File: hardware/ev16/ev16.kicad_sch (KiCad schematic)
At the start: 165 parts, among them CN1 Conn_05x02_Female, CN2 PJ-242, J1 USB_C_Receptacle, J10 Conn_01x03_Pin, J11 Conn_02x05_Counter_Clockwise, J2 Conn_01x02_Socket, J3 AudioJack4, J4 Conn_02x03_Odd_Even, J5 Conn_02x03_Odd_Even, J6 Conn_02x05_Counter_Clockwise, J7 Conn_02x05_Counter_Clockwise, J8 Conn_02x05_Counter_Clockwise, J9 Conn_02x05_Counter_Clockwise, Q1 2N7002, Q2 2N7002, SW1 SW_SPDT, SW2 SW_Push, SW3 SW_Push, SW4 SW_Push, SW5 SW_Push, SW6 SW_Push, SW7 SW_Push, U1 BQ21040DBV, U10 STM32F405RGTx, U2 USBLC6-2P6, U3 STM32F072CBTx, U4 CH340C, U5 TPS63060, U6 WM8960CGEFL/RV, U7 ESP32-S3-WROOM-1, U8 M24C02-RMN6TP, Y1 Crystal_GND24

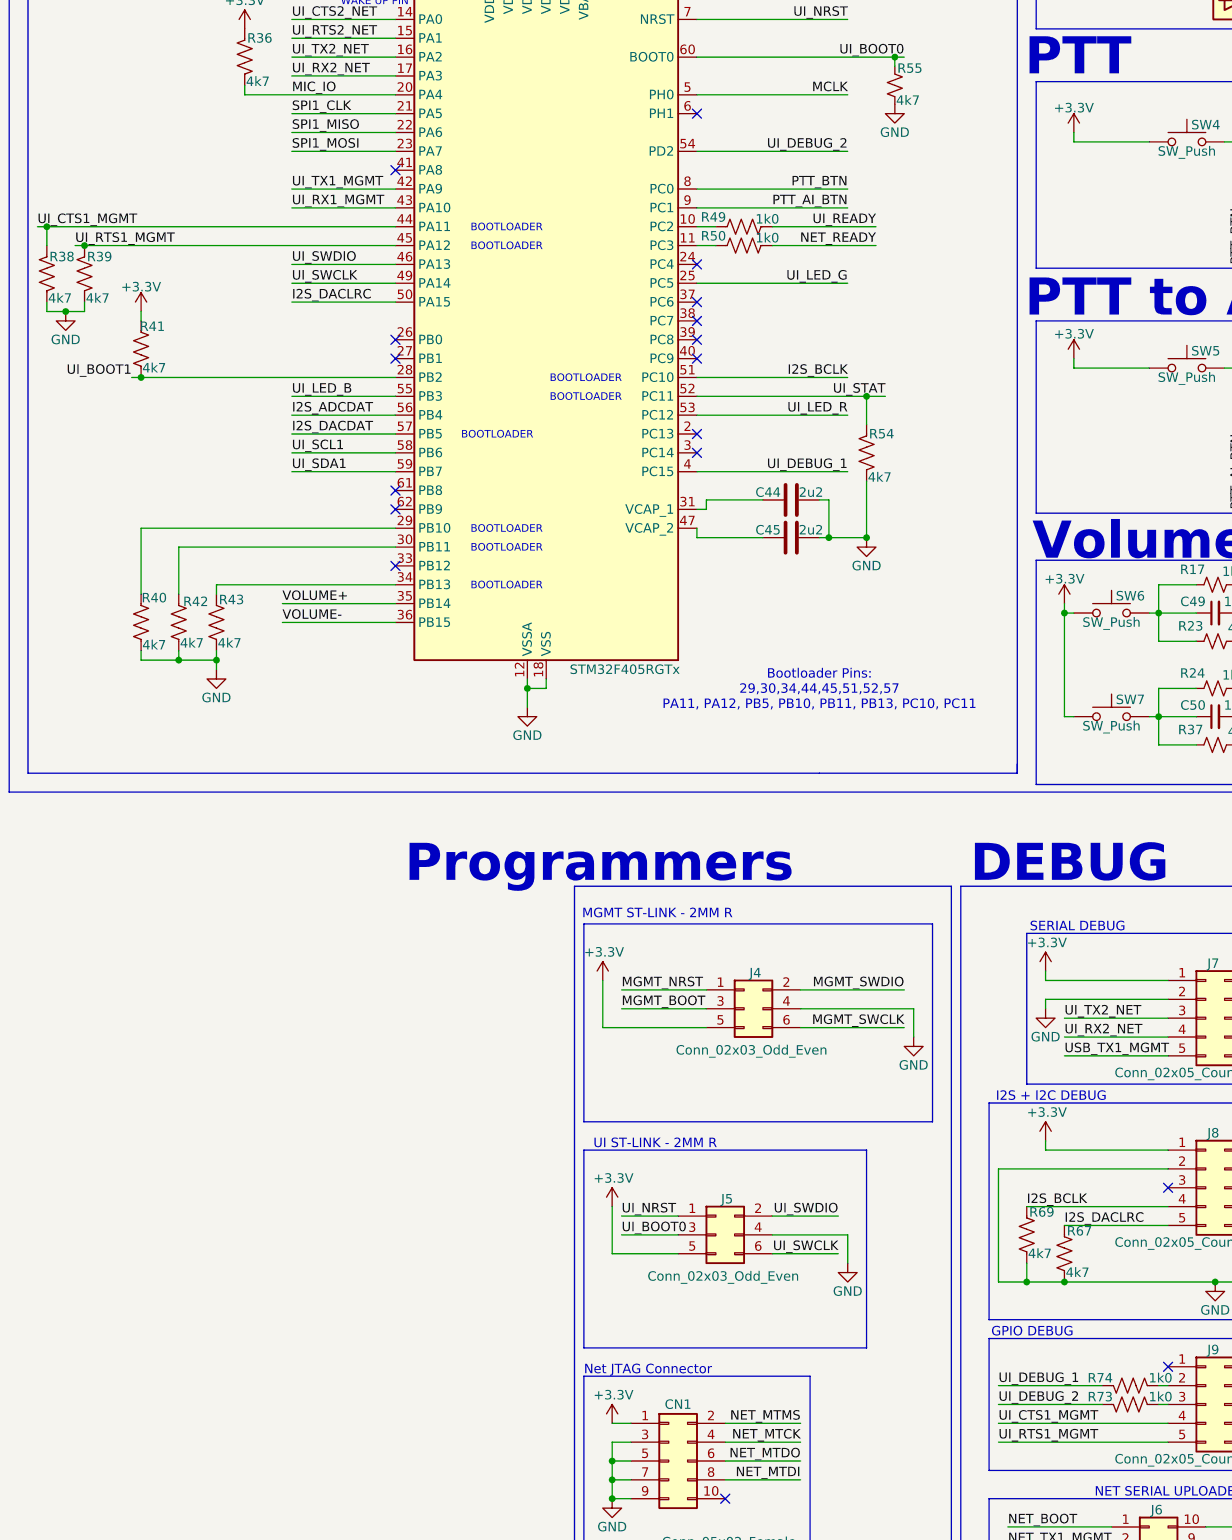
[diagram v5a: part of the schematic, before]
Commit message: stitched ground planes with vias, changed pins for volume up and down
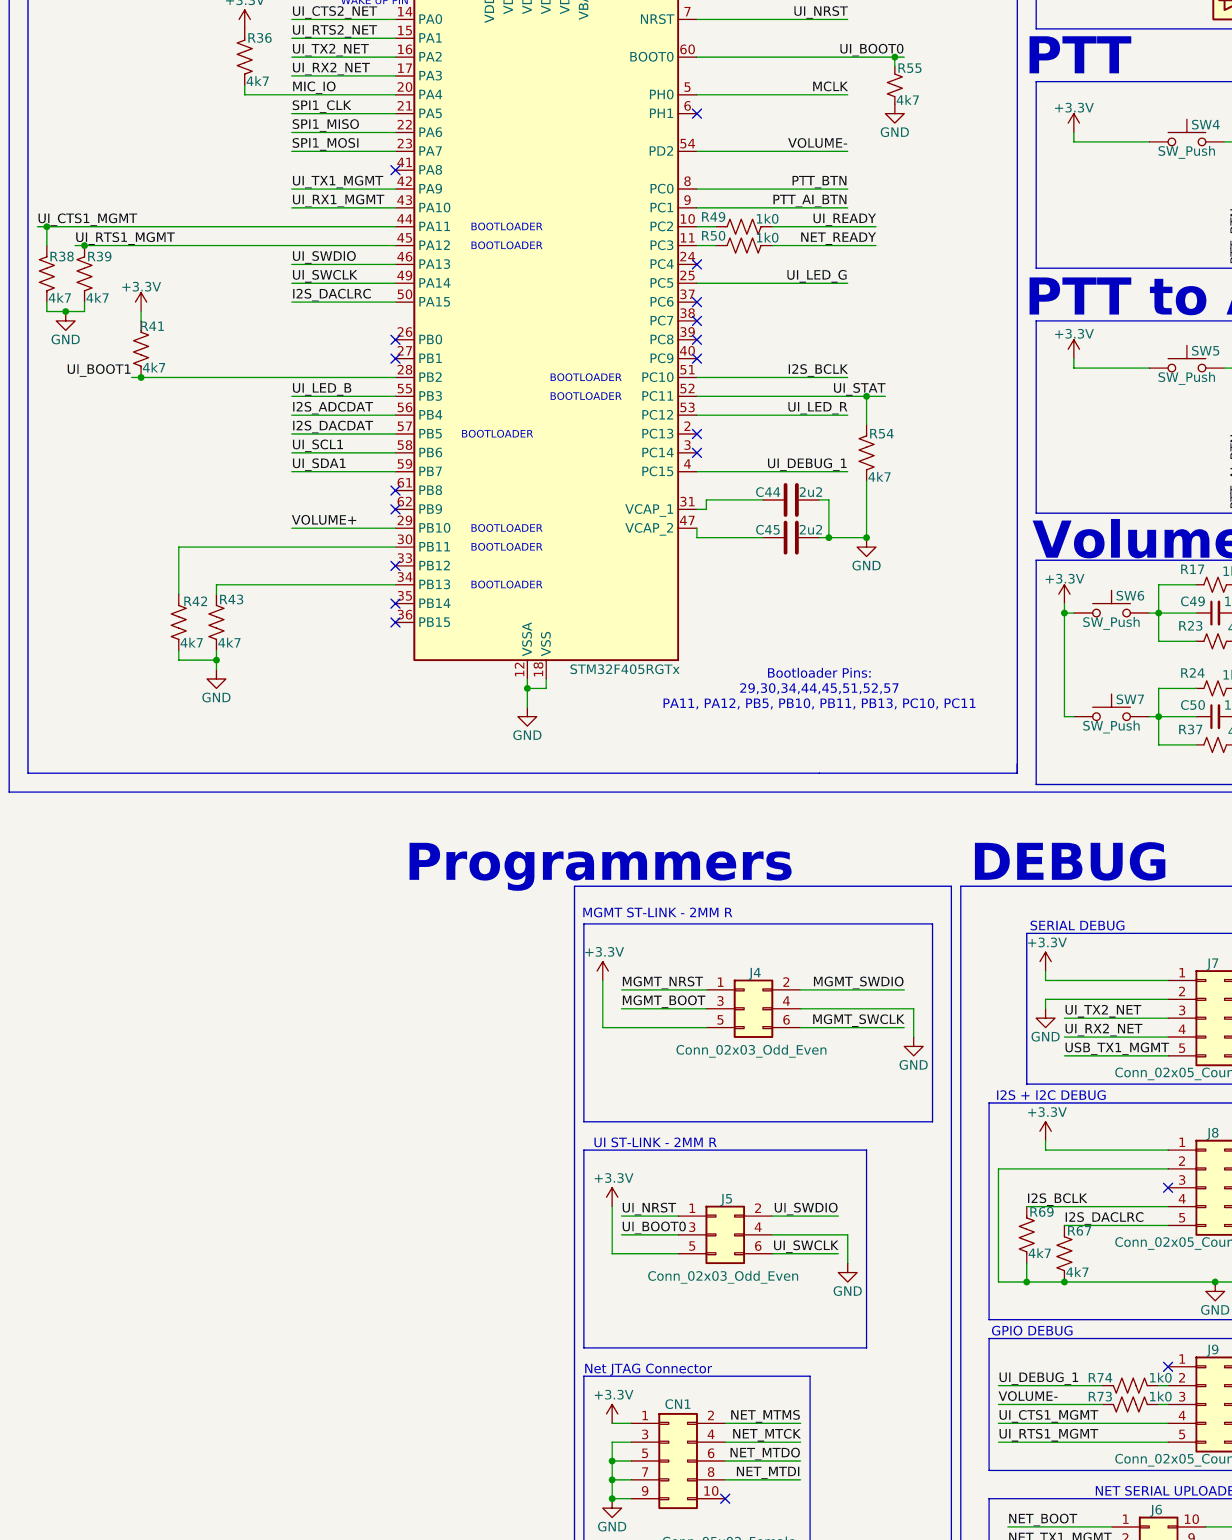
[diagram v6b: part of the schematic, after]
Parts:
- removed R40: 4k7, Resistor_SMD:R_0402_1005Metric, symbol Device:R_US
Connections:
- net UI_DEBUG_2 is gone; now on net VOLUME-: R73.2, U10.54 (PD2)
- net VOLUME+: now also U10.29 (PB10); no longer U10.35 (PB14)
- net VOLUME-: no longer U10.36 (PB15)
- no-connect marks 51 -> 53
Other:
- title: EV16 FINN BERG & BRETT REGNIER -> EV16MK1 FINN BERG & BRETT REGNIER
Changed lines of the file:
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@@
 	(paper "A2")
 	(title_block
-		(title "EV16 FINN BERG & BRETT REGNIER")
+		(title "EV16MK1 FINN BERG & BRETT REGNIER")
 		(date "2025-11-26")
-		(rev "EV16")
+		(rev "EV16MK1")
 		(company "CISCO SYSTEMS INC")
 	)
@@
 	)
 	(junction
-		(at 401.32 149.86)
-		(diameter 0)
-		(color 0 0 0 0)
-	)
-	(junction
 		(at 57.15 234.95)
 		(diameter 0)
@@
 	)
 	(no_connect
+		(at 430.53 144.78)
+	)
+	(no_connect
 		(at 57.15 247.65)
 	)
@@
 	)
 	(no_connect
+		(at 430.53 142.24)
+	)
+	(no_connect
 		(at 430.53 83.82)
 	)
@@
 	(wire
 		(pts
-			(xy 396.24 148.59) (xy 396.24 149.86)
-		)
-		(stroke
-			(width 0)
-			(type default)
-		)
-	)
-	(wire
-		(pts
 			(xy 149.86 210.82) (xy 157.48 210.82)
 		)
@@
 		)
 	)
-	(wire
-		(pts
-			(xy 396.24 132.08) (xy 430.53 132.08)
-		)
-		(stroke
-			(width 0)
-			(type default)
-		)
-	)
 	(polyline
 		(pts
@@
 	(wire
 		(pts
-			(xy 415.29 144.78) (xy 430.53 144.78)
-		)
-		(stroke
-			(width 0)
-			(type default)
-		)
-	)
-	(wire
-		(pts
 			(xy 214.63 219.71) (xy 228.6 219.71)
 		)
@@
 	(wire
 		(pts
-			(xy 415.29 142.24) (xy 430.53 142.24)
-		)
-		(stroke
-			(width 0)
-			(type default)
-		)
-	)
-	(wire
-		(pts
 			(xy 57.15 217.17) (xy 57.15 219.71)
 		)
@@
 	(wire
 		(pts
-			(xy 396.24 140.97) (xy 396.24 132.08)
-		)
-		(stroke
-			(width 0)
-			(type default)
-		)
-	)
-	(wire
-		(pts
 			(xy 287.02 200.66) (xy 292.1 200.66)
 		)
@@
 	(wire
 		(pts
-			(xy 396.24 149.86) (xy 401.32 149.86)
-		)
-		(stroke
-			(width 0)
-			(type default)
-		)
-	)
-	(wire
-		(pts
 			(xy 553.72 110.49) (xy 544.83 110.49)
 		)
@@
 	(wire
 		(pts
+			(xy 416.56 132.08) (xy 430.53 132.08)
+		)
+		(stroke
+			(width 0)
+			(type default)
+		)
+	)
+	(wire
+		(pts
 			(xy 147.32 140.97) (xy 147.32 143.51)
 		)
@@
 		)
 	)
-	(label "UI_DEBUG_2"
-		(at 511.81 250.19 0)
-		(effects
-			(font
-				(size 1.27 1.27)
-			)
-			(justify left bottom)
-		)
-	)
 	(label "LEDA_R"
 		(at 170.18 69.85 180)
@@
 		)
 	)
-	(label "VOLUME+"
-		(at 415.29 142.24 0)
-		(effects
-			(font
-				(size 1.27 1.27)
-			)
-			(justify left bottom)
-		)
-	)
 	(label "UI_SWDIO"
 		(at 490.22 224.79 180)
@@
 		)
 	)
-	(label "VOLUME-"
-		(at 415.29 144.78 0)
+	(label "BATTERY_MON"
+		(at 49.53 111.76 0)
 		(effects
 			(font
@@
 		)
 	)
-	(label "BATTERY_MON"
-		(at 49.53 111.76 0)
+	(label "UI_BOOT0"
+		(at 461.01 227.33 0)
 		(effects
 			(font
@@
 		)
 	)
-	(label "UI_BOOT0"
-		(at 461.01 227.33 0)
+	(label "VOLUME-"
+		(at 491.49 81.28 180)
 		(effects
 			(font
 				(size 1.27 1.27)
 			)
-			(justify left bottom)
+			(justify right bottom)
 		)
 	)
@@
 		)
 	)
+	(label "VOLUME+"
+		(at 416.56 132.08 0)
+		(effects
+			(font
+				(size 1.27 1.27)
+			)
+			(justify left bottom)
+		)
+	)
 	(label "NET_DEBUG_1"
 		(at 232.41 101.6 0)
@@
 		)
 	)
+	(label "VOLUME-"
+		(at 511.81 250.19 0)
+		(effects
+			(font
+				(size 1.27 1.27)
+			)
+			(justify left bottom)
+		)
+	)
 	(label "MIC_P"
 		(at 283.21 223.52 0)
@@
 		)
 	)
-	(label "UI_DEBUG_2"
-		(at 491.49 81.28 180)
-		(effects
-			(font
-				(size 1.27 1.27)
-			)
-			(justify right bottom)
-		)
-	)
 	(label "LEDA_R"
 		(at 116.84 93.98 180)
@@
 					(unit 1)
 				)
-			)
-		)
-	)
-	(symbol
-		(lib_id "Device:R_US")
-		(at 396.24 144.78 180)
-		(unit 1)
-		(exclude_from_sim no)
-		(in_bom yes)
-		(on_board yes)
-		(dnp no)
-		(property "Reference" "R40"
-			(at 398.018 141.478 0)
-			(effects
-				(font
-					(size 1.27 1.27)
-				)
-			)
-		)
-		(property "Value" "4k7"
-			(at 398.018 147.828 0)
-			(effects
-				(font
-					(size 1.27 1.27)
-				)
-			)
-		)
-		(property "Footprint" "Resistor_SMD:R_0402_1005Metric"
-			(at 398.018 144.78 90)
-			(effects
-				(font
-					(size 1.27 1.27)
-				)
-				(hide yes)
-			)
-		)
-		(property "Datasheet" "~"
-			(at 396.24 144.78 0)
-			(effects
-				(font
-					(size 1.27 1.27)
-				)
-				(hide yes)
-			)
-		)
-		(property "Description" "Resistor, US symbol"
-			(at 396.24 144.78 0)
-			(effects
-				(font
-					(size 1.27 1.27)
-				)
-				(hide yes)
-			)
-		)
-		(property "JLCPCB Part #" "C25900"
-			(at 396.24 144.78 0)
-			(effects
-				(font
-					(size 1.27 1.27)
-				)
-				(hide yes)
-			)
-		)
-		(property "Availability" ""
-			(at 396.24 144.78 0)
-			(effects
-				(font
-					(size 1.27 1.27)
-				)
-			)
-		)
-		(property "Sim.Device" ""
-			(at 396.24 144.78 0)
-			(effects
-				(font
-					(size 1.27 1.27)
-				)
-			)
-		)
-		(pin "1"
-		)
-		(pin "2"
-		)
-		(instances
-			(project "EV13 Board Design"
-				(path "/bd865368-262b-4f76-b7a6-1673c2cb0f8c"
-					(reference "R40")
-					(unit 1)
-				)

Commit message: fixed wrong jlcpcb part numbers
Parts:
- SW7: JLCPCB Part # C97448 -> C2906288
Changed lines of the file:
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@@
 			)
 		)
-		(property "JLCPCB Part #" "C97448"
+		(property "JLCPCB Part #" "C2906288"
 			(at 522.478 155.194 0)
 			(effects

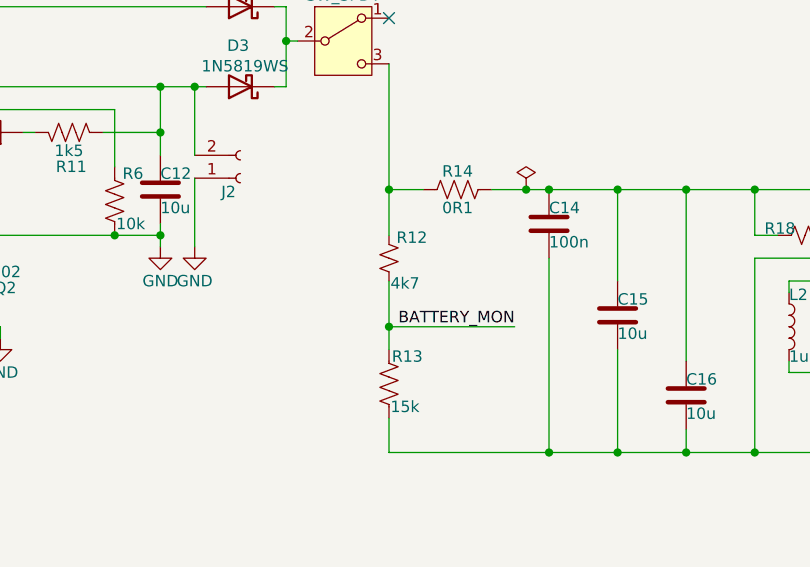
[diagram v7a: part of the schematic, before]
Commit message: Update R12 to 10k for battery monitor
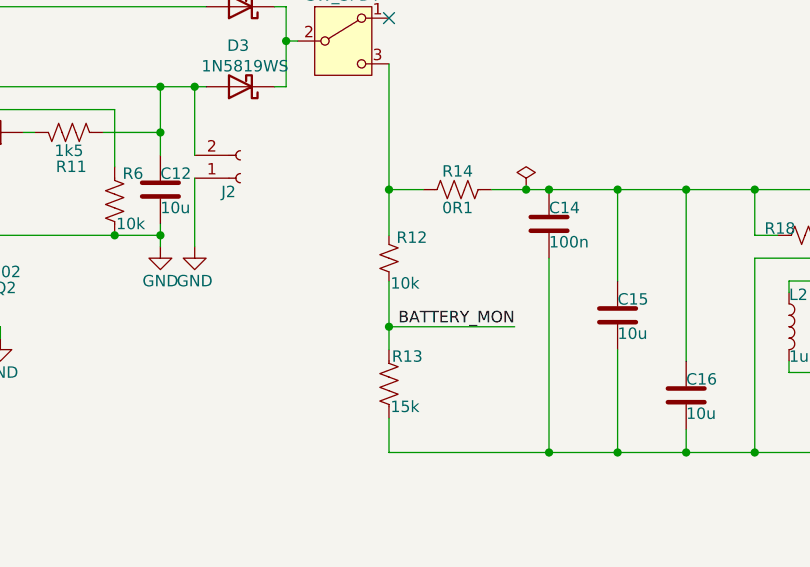
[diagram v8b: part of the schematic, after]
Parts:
- R12: value 4k7 -> 10k; JLCPCB Part # C25900 -> C25744
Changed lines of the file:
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@@
 			)
 		)
-		(property "Value" "4k7"
+		(property "Value" "10k"
 			(at 110.998 332.994 0)
 			(effects
@@
 			)
 		)
-		(property "JLCPCB Part #" "C25900"
+		(property "JLCPCB Part #" "C25744"
 			(at 109.22 330.2 0)
 			(effects
